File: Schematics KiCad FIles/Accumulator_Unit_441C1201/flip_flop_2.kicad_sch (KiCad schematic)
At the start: 16 parts, among them U1202 5963

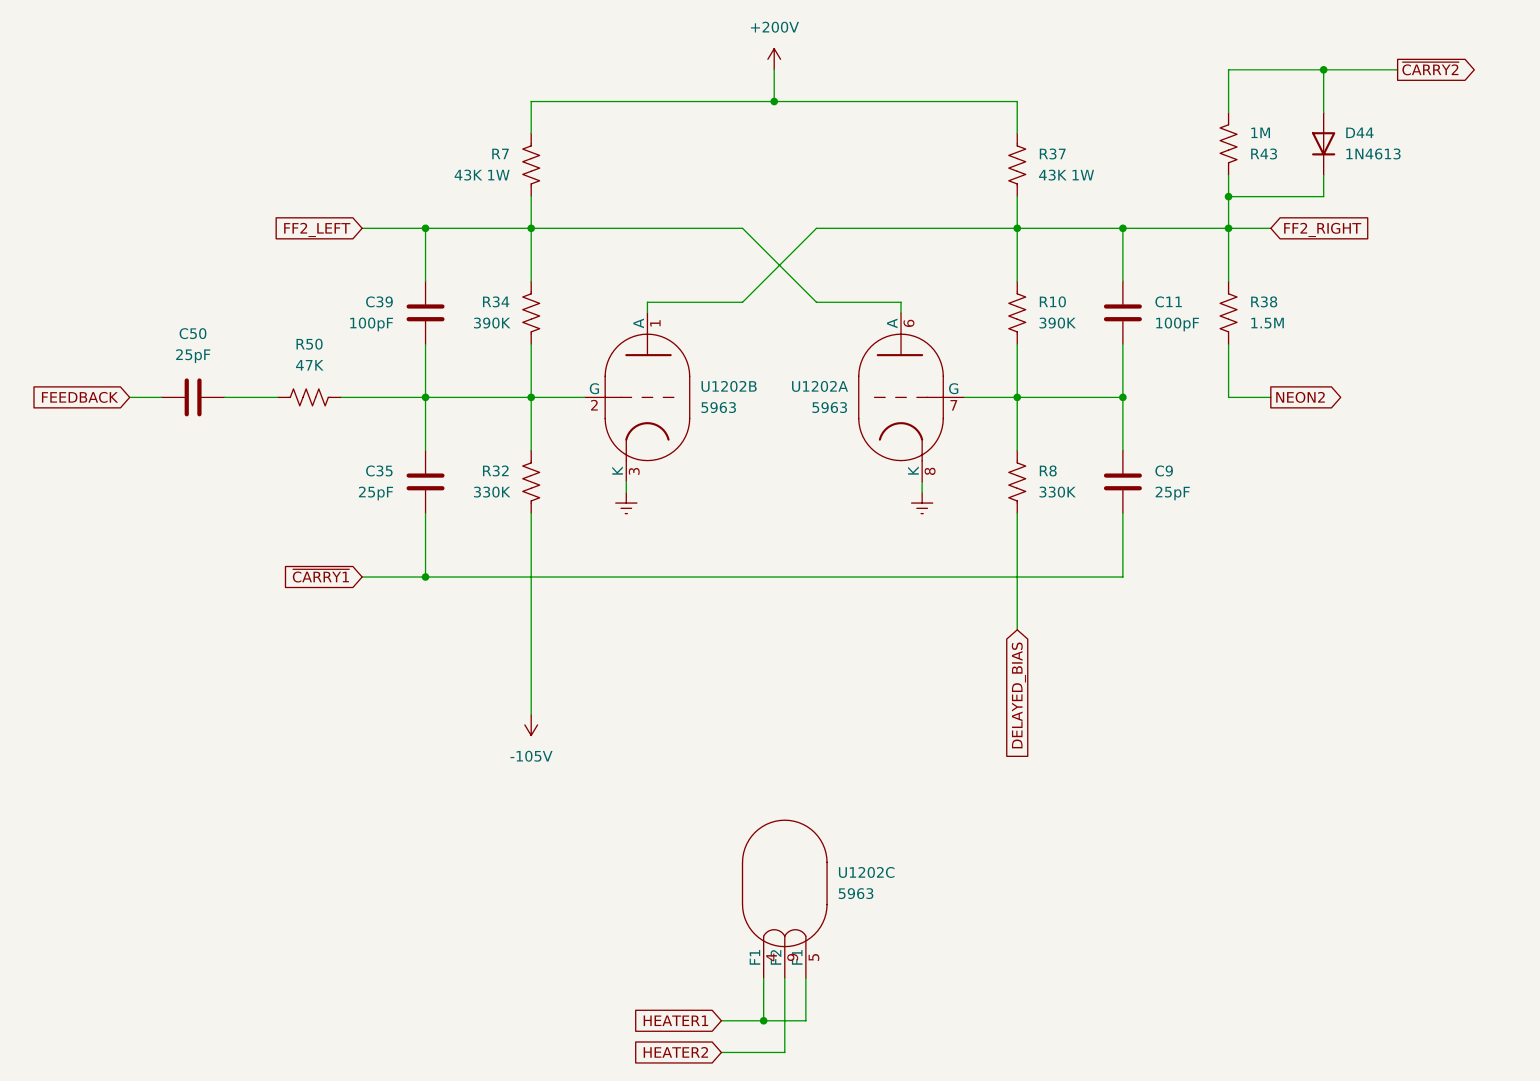
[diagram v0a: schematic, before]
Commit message: Fix component designators on accumulator schematics
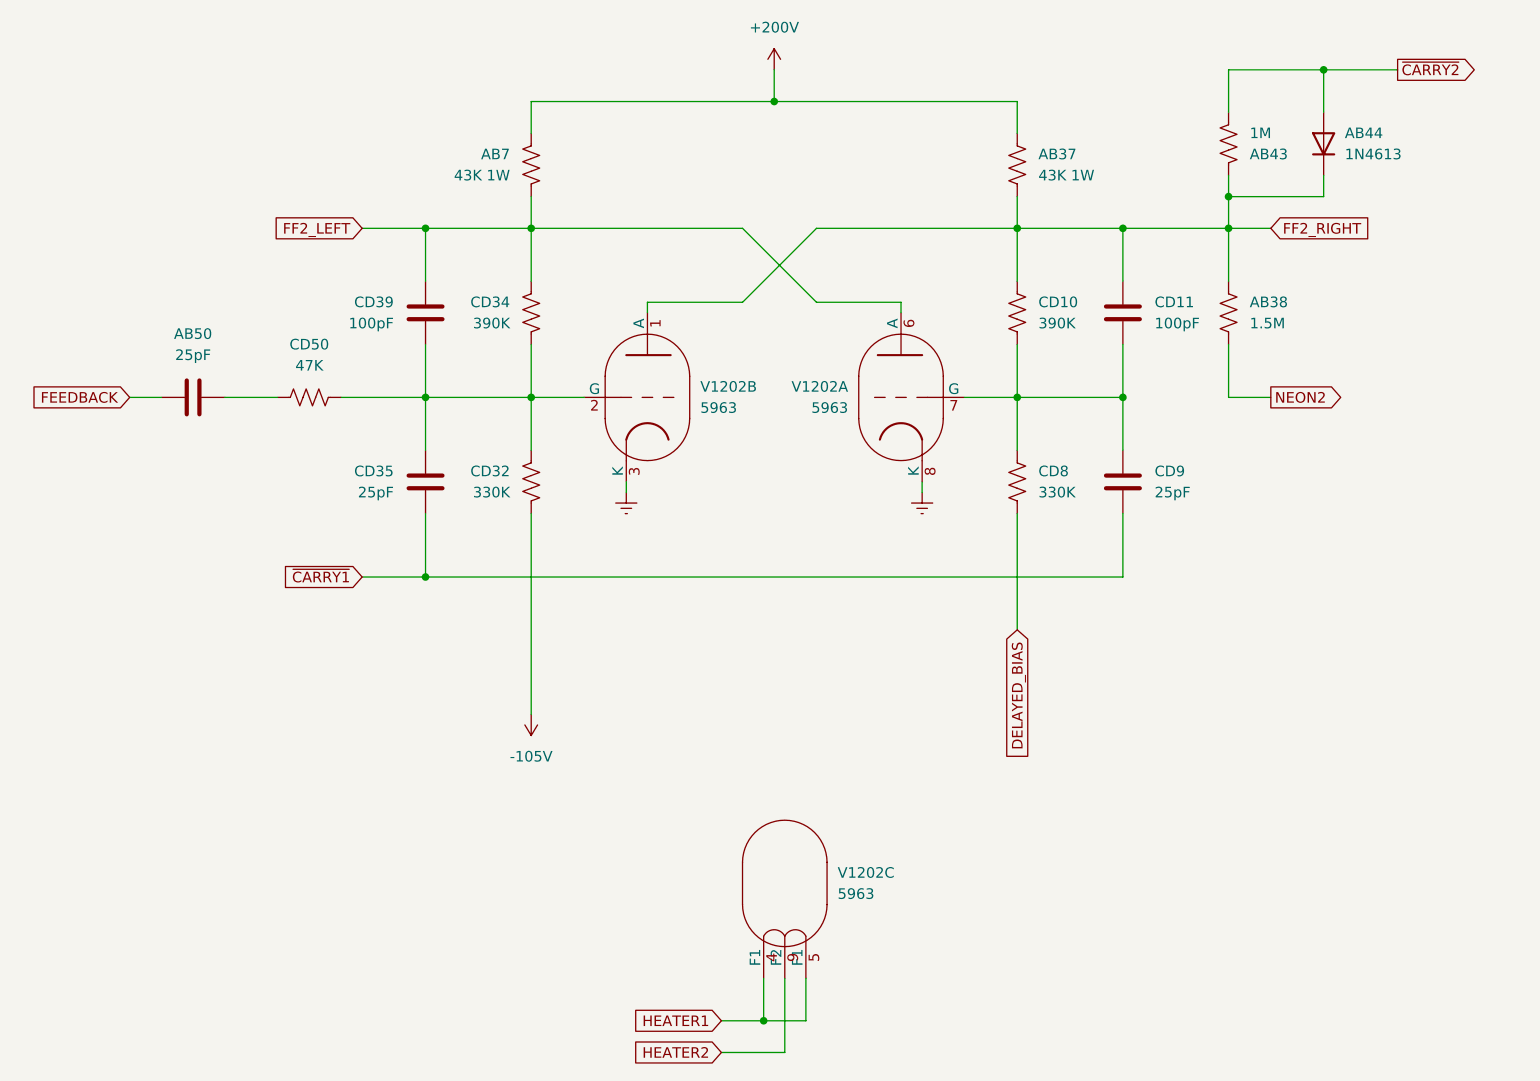
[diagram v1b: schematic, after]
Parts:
- renumbered R37 to AB37, R38 to AB38, R43 to AB43, D44 to AB44, C50 to AB50, R7 to AB7, R10 to CD10, C11 to CD11, R32 to CD32, R34 to CD34, C35 to CD35, C39 to CD39, R50 to CD50, R8 to CD8, C9 to CD9, U1202 to V1202
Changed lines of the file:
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@@
 		(on_board yes)
 		(dnp no)
-		(property "Reference" "R7"
+		(property "Reference" "AB7"
 			(at 109.22 55.8799 0)
 			(effects
@@
 			(project "Accumulator_Unit_441C1201"
 				(path "/519d7692-6bf3-45ab-bd58-713783b63e8a/f75df409-76ef-4b84-8283-0183ac39b08a"
-					(reference "R7")
+					(reference "AB7")
 					(unit 1)
 				)
@@
 		(dnp no)
 		(fields_autoplaced yes)
-		(property "Reference" "C50"
+		(property "Reference" "AB50"
 			(at 71.12 77.47 90)
 			(effects
@@
 			(project "Accumulator_Unit_441C1201"
 				(path "/519d7692-6bf3-45ab-bd58-713783b63e8a/f75df409-76ef-4b84-8283-0183ac39b08a"
-					(reference "C50")
+					(reference "AB50")
 					(unit 1)
 				)
@@
 		(on_board yes)
 		(dnp no)
-		(property "Reference" "R10"
+		(property "Reference" "CD10"
 			(at 172.72 73.6599 0)
 			(effects
@@
 			(project "Accumulator_Unit_441C1201"
 				(path "/519d7692-6bf3-45ab-bd58-713783b63e8a/f75df409-76ef-4b84-8283-0183ac39b08a"
-					(reference "R10")
+					(reference "CD10")
 					(unit 1)
 				)
@@
 		(on_board yes)
 		(dnp no)
-		(property "Reference" "R34"
+		(property "Reference" "CD34"
 			(at 109.22 73.6599 0)
 			(effects
@@
 			(project "Accumulator_Unit_441C1201"
 				(path "/519d7692-6bf3-45ab-bd58-713783b63e8a/f75df409-76ef-4b84-8283-0183ac39b08a"
-					(reference "R34")
+					(reference "CD34")
 					(unit 1)
 				)
@@
 		(on_board yes)
 		(dnp no)
-		(property "Reference" "C35"
+		(property "Reference" "CD35"
 			(at 95.25 93.9799 0)
 			(effects
@@
 			(project "Accumulator_Unit_441C1201"
 				(path "/519d7692-6bf3-45ab-bd58-713783b63e8a/f75df409-76ef-4b84-8283-0183ac39b08a"
-					(reference "C35")
+					(reference "CD35")
 					(unit 1)
 				)
@@
 		(on_board yes)
 		(dnp no)
-		(property "Reference" "U1202"
+		(property "Reference" "V1202"
 			(at 149.86 83.8199 0)
 			(effects
@@
 			(project "Accumulator_Unit_441C1201"
 				(path "/519d7692-6bf3-45ab-bd58-713783b63e8a/f75df409-76ef-4b84-8283-0183ac39b08a"
-					(reference "U1202")
+					(reference "V1202")
 					(unit 1)
 				)
@@
 		(on_board yes)
 		(dnp no)
-		(property "Reference" "C39"
+		(property "Reference" "CD39"
 			(at 95.25 73.6599 0)
 			(effects
@@
 			(project "Accumulator_Unit_441C1201"
 				(path "/519d7692-6bf3-45ab-bd58-713783b63e8a/f75df409-76ef-4b84-8283-0183ac39b08a"
-					(reference "C39")
+					(reference "CD39")
 					(unit 1)
 				)
@@
 		(on_board yes)
 		(dnp no)
-		(property "Reference" "R32"
+		(property "Reference" "CD32"
 			(at 109.22 93.9799 0)
 			(effects
@@
 			(project "Accumulator_Unit_441C1201"
 				(path "/519d7692-6bf3-45ab-bd58-713783b63e8a/f75df409-76ef-4b84-8283-0183ac39b08a"
-					(reference "R32")
+					(reference "CD32")
 					(unit 1)
 				)
@@
 		(on_board yes)
 		(dnp no)
-		(property "Reference" "R8"
+		(property "Reference" "CD8"
 			(at 172.72 93.9799 0)
 			(effects
@@
 			(project "Accumulator_Unit_441C1201"
 				(path "/519d7692-6bf3-45ab-bd58-713783b63e8a/f75df409-76ef-4b84-8283-0183ac39b08a"
-					(reference "R8")
+					(reference "CD8")
 					(unit 1)
 				)
@@
 		(on_board yes)
 		(dnp no)
-		(property "Reference" "R37"
+		(property "Reference" "AB37"
 			(at 172.72 55.8799 0)
 			(effects
@@
 			(project "Accumulator_Unit_441C1201"
 				(path "/519d7692-6bf3-45ab-bd58-713783b63e8a/f75df409-76ef-4b84-8283-0183ac39b08a"
-					(reference "R37")
+					(reference "AB37")
 					(unit 1)
 				)
@@
 		(on_board yes)
 		(dnp no)
-		(property "Reference" "R38"
+		(property "Reference" "AB38"
 			(at 198.12 73.6599 0)
 			(effects
@@
 			(project "Accumulator_Unit_441C1201"
 				(path "/519d7692-6bf3-45ab-bd58-713783b63e8a/f75df409-76ef-4b84-8283-0183ac39b08a"
-					(reference "R38")
+					(reference "AB38")
 					(unit 1)
 				)
@@
 		(on_board yes)
 		(dnp no)
-		(property "Reference" "C9"
+		(property "Reference" "CD9"
 			(at 186.69 93.9799 0)
 			(effects
@@
 			(project "Accumulator_Unit_441C1201"
 				(path "/519d7692-6bf3-45ab-bd58-713783b63e8a/f75df409-76ef-4b84-8283-0183ac39b08a"
-					(reference "C9")
+					(reference "CD9")
 					(unit 1)
 				)
@@
 		(dnp no)
 		(fields_autoplaced yes)
-		(property "Reference" "U1202"
+		(property "Reference" "V1202"
 			(at 132.08 83.8199 0)
 			(effects
@@
 			(project "Accumulator_Unit_441C1201"
 				(path "/519d7692-6bf3-45ab-bd58-713783b63e8a/f75df409-76ef-4b84-8283-0183ac39b08a"
-					(reference "U1202")
+					(reference "V1202")
 					(unit 2)
 				)
@@
 		(dnp no)
 		(fields_autoplaced yes)
-		(property "Reference" "U1202"
+		(property "Reference" "V1202"
 			(at 148.59 142.2399 0)
 			(effects
@@
 			(project "Accumulator_Unit_441C1201"
 				(path "/519d7692-6bf3-45ab-bd58-713783b63e8a/f75df409-76ef-4b84-8283-0183ac39b08a"
-					(reference "U1202")
+					(reference "V1202")
 					(unit 3)
 				)
@@
 		(on_board yes)
 		(dnp no)
-		(property "Reference" "C11"
+		(property "Reference" "CD11"
 			(at 186.69 73.6599 0)
 			(effects
@@
 			(project "Accumulator_Unit_441C1201"
 				(path "/519d7692-6bf3-45ab-bd58-713783b63e8a/f75df409-76ef-4b84-8283-0183ac39b08a"
-					(reference "C11")
+					(reference "CD11")
 					(unit 1)
 				)
@@
 		(dnp no)
 		(fields_autoplaced yes)
-		(property "Reference" "D44"
+		(property "Reference" "AB44"
 			(at 209.55 53.3399 90)
 			(effects
@@
 			(project "Accumulator_Unit_441C1201"
 				(path "/519d7692-6bf3-45ab-bd58-713783b63e8a/f75df409-76ef-4b84-8283-0183ac39b08a"
-					(reference "D44")
+					(reference "AB44")
 					(unit 1)
 				)
@@
 		(dnp no)
 		(fields_autoplaced yes)
-		(property "Reference" "R50"
+		(property "Reference" "CD50"
 			(at 85.09 78.74 90)
 			(effects
@@
 			(project "Accumulator_Unit_441C1201"
 				(path "/519d7692-6bf3-45ab-bd58-713783b63e8a/f75df409-76ef-4b84-8283-0183ac39b08a"
-					(reference "R50")
+					(reference "CD50")
 					(unit 1)
 				)
@@
 		(on_board yes)
 		(dnp no)
-		(property "Reference" "R43"
+		(property "Reference" "AB43"
 			(at 198.12 55.8801 0)
 			(effects
@@
 			(project "Accumulator_Unit_441C1201"
 				(path "/519d7692-6bf3-45ab-bd58-713783b63e8a/f75df409-76ef-4b84-8283-0183ac39b08a"
-					(reference "R43")
-					(unit 1)
-				)
+					(reference "AB43")
+					(unit 1)
+				)
